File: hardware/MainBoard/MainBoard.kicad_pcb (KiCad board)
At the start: 2 copper layers, 58.3 x 28.9 mm, 29 parts, among them J1 Therm., J2 SSR, J3 Serial, J4 5Vin, J5 SSR, J7 SSR, J8 SSR, SW1 Boot Mode, SW2 RESET, U1 ESP-12F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

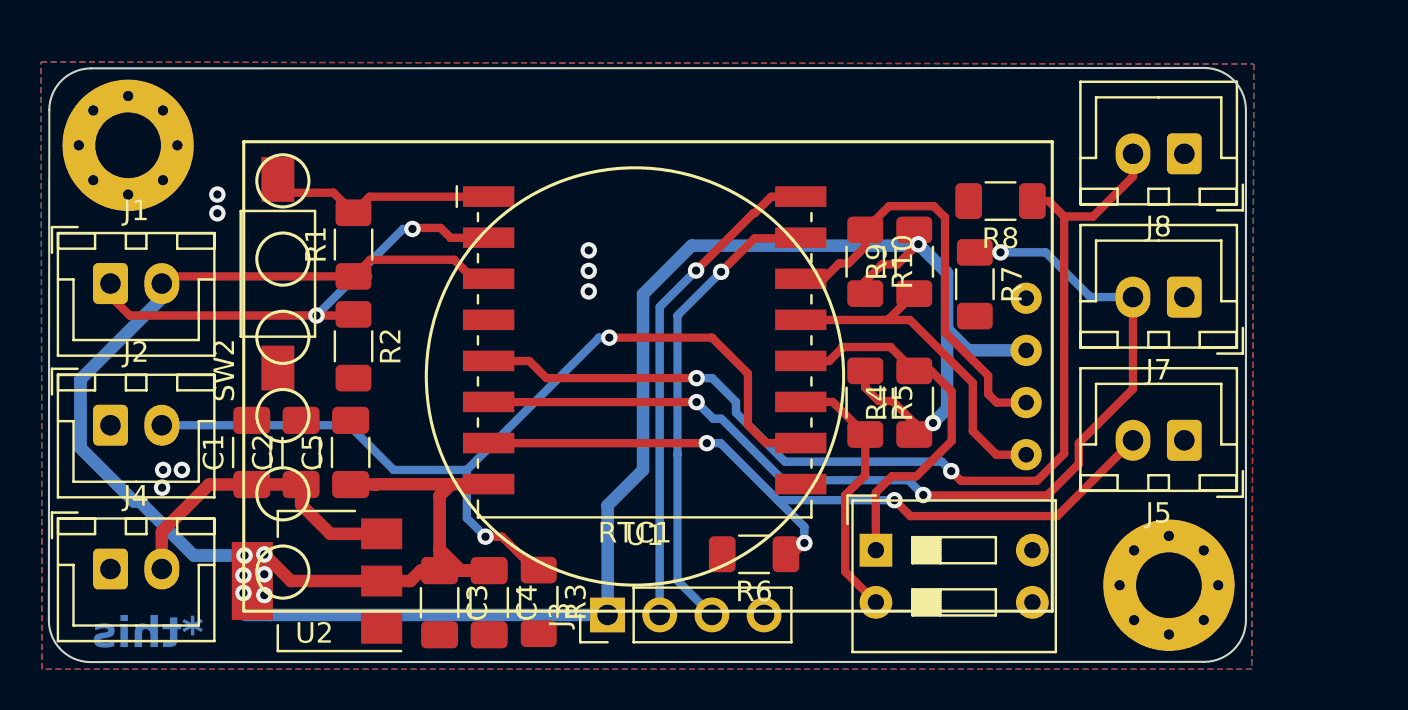
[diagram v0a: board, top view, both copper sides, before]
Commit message: led indicators added to outputs
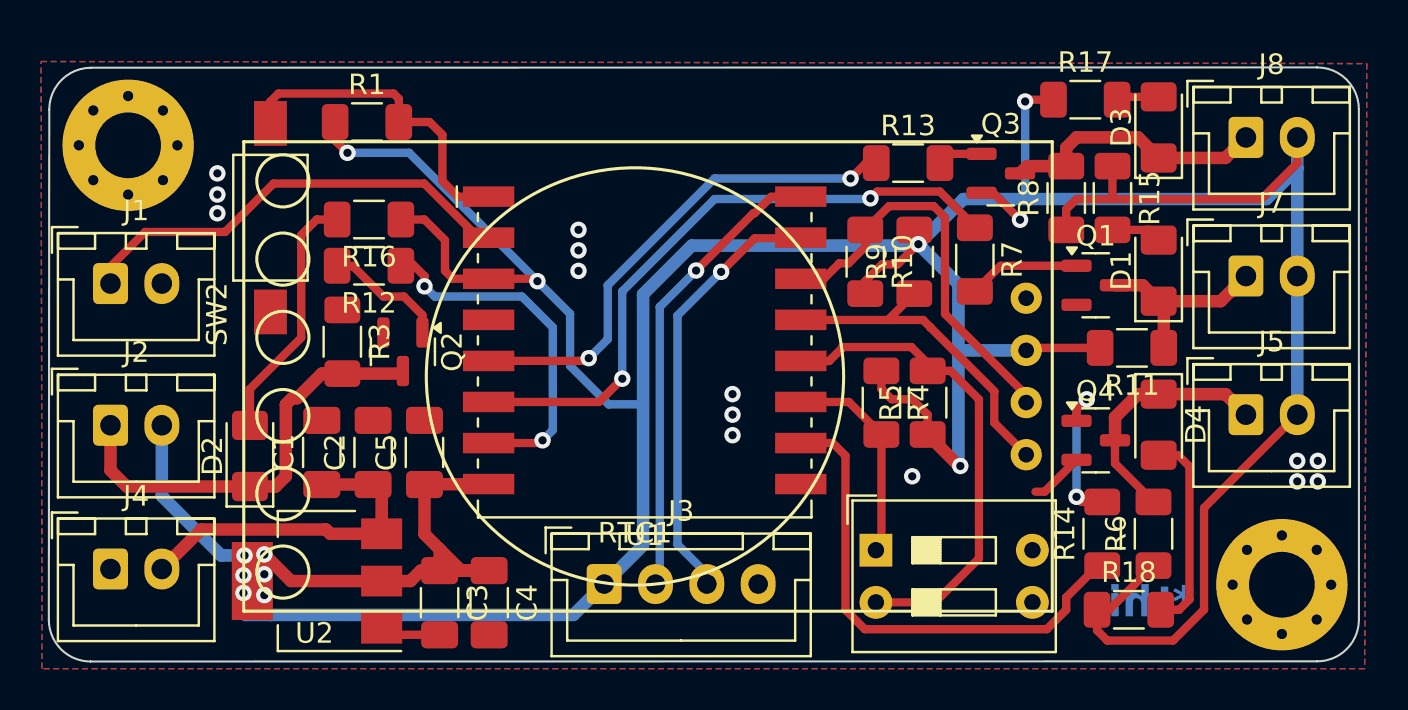
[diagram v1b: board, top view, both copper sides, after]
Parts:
- removed R2: 4.7k, Resistor_SMD:R_1206_3216Metric_Pad1.30x1.75mm_HandSolder
- added D1: LED, LED_SMD:LED_1206_3216Metric_Pad1.42x1.75mm_HandSolder, F.Cu at (66.0, 179.0)
- added D2: LED, LED_SMD:LED_1206_3216Metric_Pad1.42x1.75mm_HandSolder, F.Cu at (21.8, 188.0)
- added D3: LED, LED_SMD:LED_1206_3216Metric_Pad1.42x1.75mm_HandSolder, F.Cu at (66.0, 172.0)
- added D4: LED, LED_SMD:LED_1206_3216Metric_Pad1.42x1.75mm_HandSolder, F.Cu at (66.0, 186.5)
- added Q1: MMBT3904, Package_TO_SOT_SMD:SOT-23, F.Cu at (62.9, 179.7)
- added Q2: MMBT3904, Package_TO_SOT_SMD:SOT-23, F.Cu at (29.2, 182.9)
- added Q3: MMBT3904, Package_TO_SOT_SMD:SOT-23, F.Cu at (58.3, 174.2)
- added Q4: MMBT3904, Package_TO_SOT_SMD:SOT-23, F.Cu at (62.9, 187.2)
- added R11: 10k, Resistor_SMD:R_1206_3216Metric_Pad1.30x1.75mm_HandSolder, F.Cu at (64.7, 182.7)
- added R12: 1k, Resistor_SMD:R_1206_3216Metric_Pad1.30x1.75mm_HandSolder, F.Cu at (27.6, 178.7)
- added R13: 1k, Resistor_SMD:R_1206_3216Metric_Pad1.30x1.75mm_HandSolder, F.Cu at (53.8, 173.7)
- added R14: 1k, Resistor_SMD:R_1206_3216Metric_Pad1.30x1.75mm_HandSolder, F.Cu at (63.3, 191.8)
- added R15: 470, Resistor_SMD:R_1206_3216Metric_Pad1.30x1.75mm_HandSolder, F.Cu at (63.8, 175.4)
- added R16: 470, Resistor_SMD:R_1206_3216Metric_Pad1.30x1.75mm_HandSolder, F.Cu at (27.6, 176.5)
- added R17: 470, Resistor_SMD:R_1206_3216Metric_Pad1.30x1.75mm_HandSolder, F.Cu at (62.4, 170.6)
- added R18: 470, Resistor_SMD:R_1206_3216Metric_Pad1.30x1.75mm_HandSolder, F.Cu at (64.6, 195.5)
- J1: value Therm. -> Analog Input
- J3: footprint Connector_PinHeader_2.54mm:PinHeader_1x04_P2.54mm_Vertical -> Connector_JST:JST_XH_B4B-XH-A_1x04_P2.50mm_Vertical
- R7: value 10k -> 1k
- U1: value ESP-12F -> ESP-07
- moved R6 19.5 mm to (65.8, 191.8), turned to 90 degrees
- moved R3 15.9 mm to (26.3, 182.4)
- moved R1 6.00 mm to (27.5, 171.7), turned to 0 degrees
- moved REF** 5.50 mm to (72.0, 194.3)
- moved C5 3.59 mm to (30.3, 187.8)
- moved C2 3.51 mm to (27.8, 187.8)
- moved C1 3.41 mm to (25.3, 187.8)
- moved J5 3.25 mm to (70.3, 186.0), turned to 0 degrees
- moved R8 3.20 mm to (61.5, 175.4), turned to 90 degrees
- moved J7 3.17 mm to (70.3, 179.2), turned to 0 degrees
- moved J8 3.10 mm to (70.3, 172.5), turned to 0 degrees
- moved R5 3.04 mm to (54.8, 185.4), turned to 90 degrees
- moved SW2 2.76 mm to (22.8, 176.4)
- moved R4 1.60 mm to (52.5, 185.4), turned to -90 degrees
- moved J3 1.51 mm to (39.0, 194.2), turned to 0 degrees
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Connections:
- J1 pad 2: +3V3 -> GND
- J2 pad 1: GND -> Net-(D2-K)
- J2 pad 2: /IO15 -> +3V3
- J5 pad 1: GND -> Net-(D4-K)
- J5 pad 2: /IO13 -> +3V3
- J7 pad 1: GND -> Net-(D1-K)
- J7 pad 2: /IO12 -> +3V3
- J8 pad 1: GND -> Net-(D3-K)
- J8 pad 2: /IO14 -> +3V3
- R3 pad 1: /IO15 -> +3V3
- R3 pad 2: GND -> Net-(D2-K)
- R4 pad 2: /IO00 -> /IO02
- R5 pad 2: /IO02 -> /IO00
- R6 pad 1: /IO13 -> +3V3
- R6 pad 2: GND -> Net-(D4-K)
- R7 pad 2: GND -> Net-(Q1-B)
- R8 pad 1: /IO14 -> +3V3
- R8 pad 2: GND -> Net-(D3-K)
- SW1 pad 1: /IO00 -> /IO02
- SW1 pad 2: /IO02 -> /IO00
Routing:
- net +3V3: track 146.4 -> 229.3 mm, vias 8 -> 11
- net /IO14: track 50.2 -> 24.6 mm
- net Net-(D2-K): track 0.00 -> 21.1 mm
- net /IO13: track 38.1 -> 17.0 mm, vias 3 -> 2
- net /IO15: track 45.3 -> 24.5 mm, vias 2 -> 0
- net /IO12: track 49.1 -> 31.2 mm, vias 3 -> 2
- net Net-(D3-K): track 0.00 -> 13.1 mm
- net Net-(D2-A): track 0.00 -> 12.4 mm
- net Net-(D4-K): track 0.00 -> 12.2 mm
- net Net-(D4-A): track 0.00 -> 9.81 mm
- net Net-(D1-K): track 0.00 -> 9.58 mm
- net GND: track 0.00 -> 8.50 mm, vias 8 -> 15
- net Net-(Q4-B): track 0.00 -> 7.57 mm, vias 0 -> 2
- net Net-(Q2-B): track 0.00 -> 6.11 mm
- net Net-(Q1-B): track 0.00 -> 5.47 mm
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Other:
- board size 58.3 x 28.9 mm -> 63.8 x 28.9 mm
- board text removed: "TODO: add transistors to drive relays and add leds for outputs"

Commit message: gsm board module designed
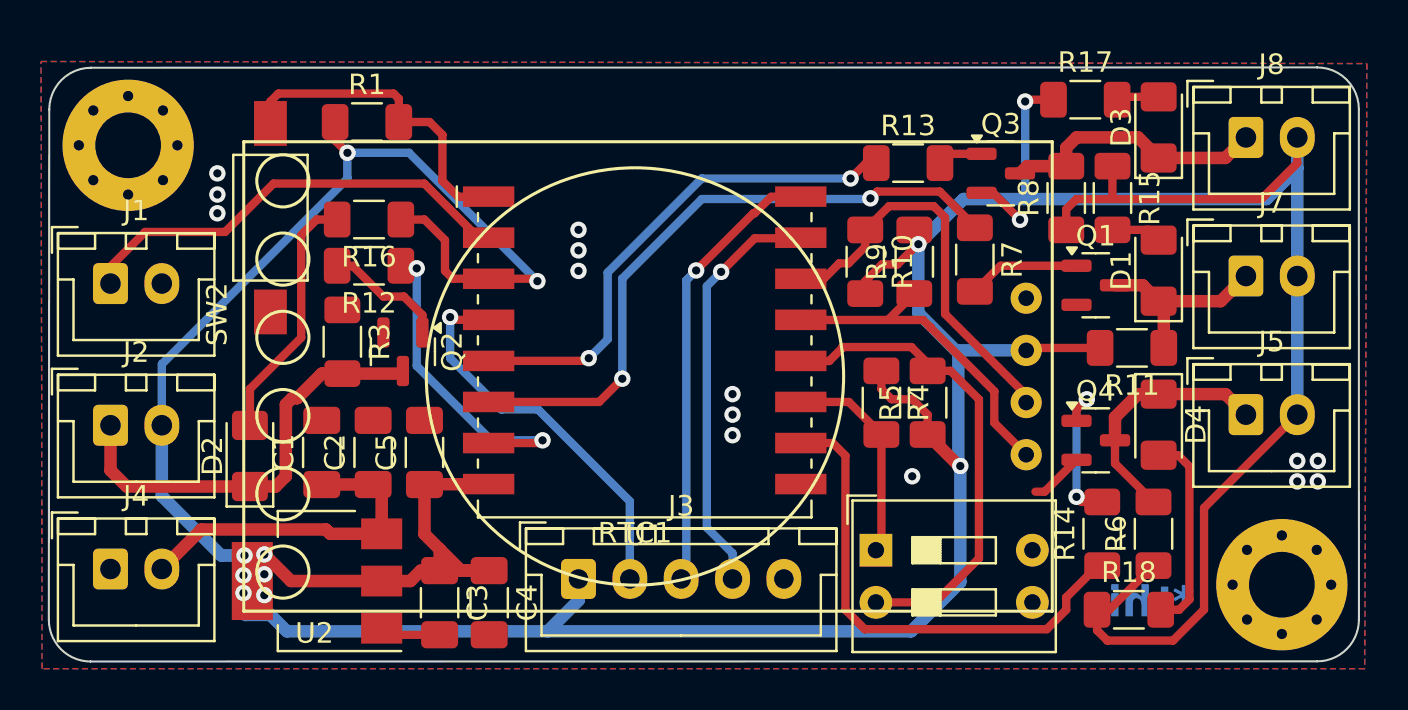
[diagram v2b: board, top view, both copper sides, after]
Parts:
- J3: footprint Connector_JST:JST_XH_B4B-XH-A_1x04_P2.50mm_Vertical -> Connector_JST:JST_XH_B5B-XH-A_1x05_P2.50mm_Vertical
- moved J3 1.27 mm to (37.8, 194.0)
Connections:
- J3 pad 2: /TX -> /IO16
- J3 pad 3: /RX -> /TX
- J3 pad 4: GND -> /RX
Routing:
- net /IO16: track 0.00 -> 19.3 mm, vias 0 -> 1
- net +3V3: track 229.3 -> 235.3 mm
- net /IO13: track 17.0 -> 15.6 mm
- net /RX: track 21.2 -> 20.3 mm
- net /TX: track 22.7 -> 21.9 mm
